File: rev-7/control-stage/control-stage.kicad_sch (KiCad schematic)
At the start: 65 parts, among them U1 REF4132A33, U2 ADP1706, U3 STM32G474RBTx, U4 LT3040, Y1 Crystal_GND24

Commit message: RC1 schematic + footprints
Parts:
- removed U1: REF4132A33, symbol rev-7-symbols:REF4132
- removed U4: LT3040, symbol rev-7-symbols:LT3040
- removed U?: (no value), symbol rev-7-symbols:ADP1706
- added C47, C48: DNP, Capacitor_SMD:C_0402_1005Metric, symbol Device:C_Small
- added C49: (no value), Capacitor_SMD:C_0402_1005Metric, symbol Device:C_Small
- added C50, C51, C52: (no value), symbol Device:C_Small
- added J5: (no value), symbol Connector_Generic:Conn_02x05_Counter_Clockwise
- added NT1: NetTie_2, symbol Device:NetTie_2
- added NT2: (no value), symbol Device:NetTie_2
- added R5, R8: (no value), symbol Device:R_Small_US
- added R6, R7, R9: 0, symbol Device:R_Small_US
- added U1: (no value), symbol rev-7-symbols:ADP7156ACPZ
- added U4: (no value), symbol Amplifier_Operational:TLV9004xRUCR
- C11, C9: value 20p -> (none); footprint Capacitor_SMD:C_0603_1608Metric -> (none)
- C22, C8: value 100n -> (none)
- C25: value 4.7u -> (none)
- C26: value 4.7u -> 1u
- C28: value 100n -> 1u
- C31: value 2.2u -> DNP; footprint (none) -> Capacitor_SMD:C_0402_1005Metric
- C5: value 4.7u -> (none); footprint (none) -> Capacitor_SMD:C_1210_3225Metric; P/N (none) -> GRM32EC81C476ME15L
- R2: value 200k -> (none)
- R3: value 5.1k -> (none)
- R4: value 499 -> (none)
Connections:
- net +3V3: now also J5.1 (Pin_1)
- net +3V3A: now also R4.2, C50.1, C51.1, C52.1, R5.1, U1.1 (VOUT), U1.2 (VOUT), U1.3 (VOUT_SENSE), U4.3 (V+)
- net +5V: now also J5.10 (Pin_10)
- net BOOT0: now also U3.61 (PB8), J5.8 (Pin_8)
- net CAN_RX: now also U3.58 (PB5); no longer U3.30 (PB10)
- net CAN_TX: now also U3.59 (PB6); no longer U3.62 (PB9)
- net DEBUG_RX: now also J5.7 (Pin_7)
- net DEBUG_SWCLK: now also J5.2 (Pin_2)
- net DEBUG_SWDIO: now also J5.9 (Pin_9)
- net DEBUG_TX: now also J5.4 (Pin_4)
- net EP: now also C31.2, R3.1, C47.2, C48.2, C49.2, C50.2, C51.2, C52.2, J5.5 (Pin_5), J5.6 (Pin_6), NT2.1, U1.11 (GND), U4.10 (V-); no longer C31.1, R4.1
- net NRST: now also J5.3 (Pin_3)
- net PGND: now also NT2.2
- net PHA_ISNS: now also U4.2 (+); no longer U3.12 (PA0)
- net PHB_ISNS: now also U4.4 (+); no longer U3.13 (PA1)
- net PHC_ISNS: now also U4.9 (+); no longer U3.25 (PB1)
- net THERM_A: now also R5.2
- net THERM_B: now also R4.1
- net VBUS: now also NT1.1
- net VBUS_VSNS: now also C5.1, R2.2, R3.2, U4.11 (+); no longer U3.36 (PB14)
- net V+: no longer names the net of C21.1, C7.1, C8.1, FB2.2
- net V+: now also C22.1, U1.10 (VIN), U1.5 (EN), U1.9 (VIN); no longer C25.1, C28.1, C5.1, R2.1
- new net: NT1.2, R2.1
- new net: R6.2, U4.1 (-), U4.14
- new net: R9.2, U4.5 (-), U4.6
- new net: R8.2, U4.12 (-), U4.13
- new net: C25.1, U1.4 (BYP)
- new net: C28.1, U1.6 (REF_SENSE), U1.7 (REF)
- new net: C26.1, U1.8 (VREG)
- new net: R7.2, U4.7, U4.8 (-)
- new net PHA_ISNS_BUF: C31.1, R6.1, U3.12 (PA0)
- new net PHB_ISNS_BUF: C47.1, R9.1, U3.13 (PA1)
- new net PHC_ISNS_BUF: C48.1, R7.1, U3.25 (PB1)
- new net VBUS_VSNS_BUF: C49.1, R8.1, U3.36 (PB14)
- no-connect marks 0 -> 22
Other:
- note added: "3V3 Analog LDO"
- note added: "3V3 Digital LDO"
- note added: "Analog"
- note added: "Analog Buffers"
- note added: "Debug"
- note added: "Inverter board +5V switch"
- note added: "Mezz plugs to inverter board"
- note added: "Op amp power"
- note added: "Phase/SPI"
- note added: "Power"
- note added: "STM32"
- note added: "Star at mezz"
- note added: "Up to 120mA draw - ~100-200mW TODO do we have the thermal conductivity for this not to be a problem? Should we use SMPS buck?"
- note removed: "3V3 +/- 2.5% 1A max"
- note removed: "hehe centipede"
- moved on the sheet: C1, C10, C11, C12, C13, C14, C15, C16, C17, C18, C19, C2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

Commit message: Design review changes
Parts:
- removed C10: 4.7u, symbol Device:C_Small
- removed C36: 22u, symbol Device:C_Small
- added C?: 4.7u, Capacitor_SMD:C_0603_1608Metric, symbol Device:C_Small
- added C?: 100n, Capacitor_SMD:C_0603_1608Metric, symbol Device:C_Small
- added R?: 120, Resistor_SMD:R_0603_1608Metric, symbol Device:R_Small_US
- added U?: TCAN330, project-footprints:SOT-23-8-Fixed, symbol Interface_CAN_LIN:TCAN330
- C11, C9: value (none) -> 18p; footprint (none) -> Capacitor_SMD:C_0402_1005Metric
- C12, C14, C52, C8: value (none) -> 4.7u; footprint (none) -> Capacitor_SMD:C_0603_1608Metric
- C13, C21, C3, C33, C34, C39, C4, C40, C41, C42: footprint (none) -> Capacitor_SMD:C_0603_1608Metric
- C15, C18, C26, C27, C28, C29, C30, C32, C38: footprint (none) -> Capacitor_SMD:C_0402_1005Metric
- C16: value (none) -> 10u; footprint (none) -> Capacitor_SMD:C_0603_1608Metric
- C17, C25, C37: value (none) -> 1u; footprint (none) -> Capacitor_SMD:C_0402_1005Metric
- C20: value (none) -> 1u; footprint (none) -> Capacitor_SMD:C_0603_1608Metric
- C22, C23, C24, C51: value (none) -> 100n; footprint (none) -> Capacitor_SMD:C_0402_1005Metric
- C35, C50: value (none) -> 10n; footprint (none) -> Capacitor_SMD:C_0402_1005Metric
- C43: footprint (none) -> Capacitor_SMD:C_0805_2012Metric
- C49: value (none) -> DNP
- C5: value (none) -> 10p
- FB1, FB2, FB4: footprint (none) -> Inductor_SMD:L_0603_1608Metric
- FB3: value (none) -> Z@1MHz=300ohm; footprint (none) -> Inductor_SMD:L_0603_1608Metric
- J1: value (none) -> MEZZ; footprint (none) -> rev-7-footprints:0555600307
- J2, J3, J4: value (none) -> 10132797-021100LF; footprint (none) -> rev-7-footprints:10132798-021100LF
- J5: value (none) -> PROG; footprint (none) -> Connector:Tag-Connect_TC2050-IDC-NL_2x05_P1.27mm_Vertical_with_bottom_clip
- NT1: footprint (none) -> NetTie:NetTie-2_SMD_Pad0.5mm
- NT2: value (none) -> NetTie_2; footprint (none) -> NetTie:NetTie-2_SMD_Pad0.5mm
- Q1: value (none) -> TPN4R712MD,L1Q; footprint (none) -> rev-7-footprints:TSON-Advance
- R1: value (none) -> 100k; footprint (none) -> Resistor_SMD:R_0402_1005Metric
- R2: value (none) -> 5.1k/0.1%; footprint (none) -> Resistor_SMD:R_0402_1005Metric
- R3: value (none) -> 3.3k/0.1%; footprint (none) -> Resistor_SMD:R_0402_1005Metric
- R4, R5: value (none) -> 100k/1%; footprint (none) -> Resistor_SMD:R_0402_1005Metric
- R6, R7, R9: footprint (none) -> Resistor_SMD:R_0402_1005Metric
- R8: value (none) -> 0; footprint (none) -> Resistor_SMD:R_0402_1005Metric
- U1: value (none) -> ADP7156ACPZ; footprint (none) -> Package_DFN_QFN:DFN-10-1EP_3x3mm_P0.5mm_EP1.55x2.48mm
- U4: value (none) -> TLV9154IRUCR; footprint (none) -> Package_DFN_QFN:Texas_S-PX2QFN-14
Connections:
- net IA_SNS is gone; now on net PHA_ISNS: J4.16 (Pin_16), J4.5 (Pin_5)
- net IB_SNS is gone; now on net PHB_ISNS: J4.14 (Pin_14), J4.7 (Pin_7)
- net IC_SNS is gone; now on net PHC_ISNS: J4.12 (Pin_12), J4.9 (Pin_9)
- net +3V3: now also C?.1, C?.1, U?.3 (VCC)
- net CAN_H: now also U?.7 (CANH)
- net CAN_L: now also U?.6 (CANL)
- net CAN_RX: now also U?.4 (RXD)
- net CAN_TX: now also U?.1 (TXD)
- net ENC_A: now also U3.8 (PC0)
- net ENC_B: now also U3.9 (PC1)
- net EP: now also C?.2, C?.2, U?.2 (GND), U?.8 (S)
- net SW_5V: now also U3.60 (PB7); no longer U3.34 (PB12)
- no-connect marks 22 -> 21
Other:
- note added: "5V tolerant"
- note added: "System Communications"
- moved on the sheet: C46, C5, R2, R3

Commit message: Pushing changes to rev7
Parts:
- removed C44, C45, C46: 47u, Capacitor_SMD:C_1210_3225Metric, symbol Device:C_Small
- removed C52: 4.7u, Capacitor_SMD:C_0603_1608Metric, symbol Device:C_Small
- removed J5: PROG, Connector:Tag-Connect_TC2050-IDC-NL_2x05_P1.27mm_Vertical_with_bottom_clip, symbol Connector_Generic:Conn_02x05_Counter_Clockwise
- removed R?: 120, Resistor_SMD:R_0603_1608Metric, symbol Device:R_Small_US
- added H1: Board_Def, rev-7-footprints:top-board-def, symbol Mechanical:MountingHole_Pad
- added J5: Hirose_FH12-10S-0.5SH, Connector_FFC-FPC:Hirose_FH12-10S-0.5SH_1x10-1MP_P0.50mm_Horizontal, symbol Connector_Generic_MountingPin:Conn_01x10_MountingPin
- U1: footprint Package_DFN_QFN:DFN-10-1EP_3x3mm_P0.5mm_EP1.55x2.48mm -> Package_DFN_QFN:DFN-10-1EP_3x3mm_P0.5mm_EP1.65x2.38mm
- U2: footprint (none) -> rev-7-footprints:DFN-8-1EP_3x3mm_P0.5mm_EP1.45x1.74mm
- U5: renamed from U?; footprint project-footprints:SOT-23-8-Fixed -> rev-7-footprints:SOT-23-8-Fixed
- gave numbers to parts that had none: 2
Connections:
- net +3V3: now also J5.1 (Pin_1)
- net +5V: now also J5.2 (Pin_2)
- net BOOT0: now also J5.7 (Pin_7)
- net DEBUG_RX: now also J5.9 (Pin_9)
- net DEBUG_SWCLK: now also J5.4 (Pin_4)
- net DEBUG_SWDIO: now also J5.5 (Pin_5)
- net DEBUG_TX: now also J5.8 (Pin_8)
- net NRST: now also J5.6 (Pin_6)
- net BYP: now reaches C25.1, U1.4 (BYP)
- net REF: now reaches C28.1, U1.6 (REF_SENSE), U1.7 (REF)
- net VREG: now reaches C26.1, U1.8 (VREG)
- net EP renamed GND
- net GND: now also J5.10 (Pin_10), J5.3 (Pin_3), J5.MP (MountPin)
- new net CHASSIS: H1.1
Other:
- note removed: "System Communications"

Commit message: Updating
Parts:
- removed C31, C47, C48, C49: DNP, Capacitor_SMD:C_0402_1005Metric, symbol Device:C_Small
- removed C50: 10n, Capacitor_SMD:C_0402_1005Metric, symbol Device:C_Small
- removed C51: 100n, Capacitor_SMD:C_0402_1005Metric, symbol Device:C_Small
- removed R6, R7, R8, R9: 0, Resistor_SMD:R_0402_1005Metric, symbol Device:R_Small_US
- removed U4: TLV9154IRUCR, Package_DFN_QFN:Texas_S-PX2QFN-14, symbol Amplifier_Operational:TLV9004xRUCR
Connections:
- net PHA_ISNS_BUF is gone; now on net PHA_ISNS: U3.12 (PA0)
- net PHB_ISNS_BUF is gone; now on net PHB_ISNS: U3.13 (PA1)
- net PHC_ISNS_BUF is gone; now on net PHC_ISNS: U3.25 (PB1)
- net VBUS_VSNS_BUF is gone; now on net VBUS_VSNS: U3.36 (PB14)
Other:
- note added: "Swap with MEMS?"
- note removed: "Analog Buffers"
- note removed: "Op amp power"

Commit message: Rev 7 RC1 - Push before design review
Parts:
- removed C21, C33, C34, C40, C41, C42: 4.7u, Capacitor_SMD:C_0603_1608Metric, symbol Device:C_Small
- removed C30: 100n, Capacitor_SMD:C_0402_1005Metric, symbol Device:C_Small
- removed C39: 10u, Capacitor_SMD:C_0603_1608Metric, symbol Device:C_Small
- removed C43: 22u, Capacitor_SMD:C_0805_2012Metric, symbol Device:C_Small
- removed FB2: Z@1MHz=100ohm, Inductor_SMD:L_0603_1608Metric, symbol Device:FerriteBead_Small
- removed FB3, FB4: Z@1MHz=300ohm, Inductor_SMD:L_0603_1608Metric, symbol Device:FerriteBead_Small
- removed NT1: NetTie_2, NetTie:NetTie-2_SMD_Pad0.5mm, symbol Device:NetTie_2
- removed U2: ADP1706, rev-7-footprints:DFN-8-1EP_3x3mm_P0.5mm_EP1.45x1.74mm, symbol rev-7-symbols:ADP1706
- added L1: 2.2u, Inductor_SMD:L_1008_2520Metric, symbol Device:L
- added NT3: NetTie_2, NetTie:NetTie-2_SMD_Pad0.5mm, symbol Device:NetTie_2
- added R10: 100k/1%, Resistor_SMD:R_0402_1005Metric, symbol Device:R_Small_US
- added R11, R12, R13, R14, R15, R16, R17, R18, R19: THJP0603ABT1, Resistor_SMD:R_0603_1608Metric, symbol Device:R_Small_US
- added R6, R7: 10k, Resistor_SMD:R_0402_1005Metric, symbol Device:R_Small_US
- added R8: 2.2, Resistor_SMD:R_0603_1608Metric, symbol Device:R_Small_US
- added R9: 442k/1%, Resistor_SMD:R_0402_1005Metric, symbol Device:R_Small_US
- added U2: TLV62569DRL, Package_TO_SOT_SMD:SOT-563, symbol Regulator_Switching:TLV62569DRL
- C10, C4, C8: value 4.7u -> 10u; P/N (none) -> GRT188R61C106KE13
- C11, C9: value 18p -> 20p
- C12, C13: value 4.7u -> 22u; P/N (none) -> GRT188C80J226ME13D
- C15: value 100n -> 22u; footprint Capacitor_SMD:C_0402_1005Metric -> Capacitor_SMD:C_0603_1608Metric; P/N (none) -> GRT188C80J226ME13D
- C16: value 10u -> 22u; P/N (none) -> GRT188C80J226ME13D
- C17: value 1u -> 22u; footprint Capacitor_SMD:C_0402_1005Metric -> Capacitor_SMD:C_0603_1608Metric; P/N (none) -> GRT188C80J226ME13D
- C18: value 10n -> DNP
- C20, C36: footprint Capacitor_SMD:C_0603_1608Metric -> Capacitor_SMD:C_0402_1005Metric
- C24: value 100n -> 10n
- C3: value 4.7u -> 100n; footprint Capacitor_SMD:C_0603_1608Metric -> Capacitor_SMD:C_0402_1005Metric
- C5: footprint Capacitor_SMD:C_1210_3225Metric -> Capacitor_SMD:C_0402_1005Metric
- C6, C7: value 47u -> 10u; footprint Capacitor_SMD:C_1210_3225Metric -> Capacitor_SMD:C_0603_1608Metric; P/N GRM32EC81C476ME15L -> GRT188R61C106KE13
- FB1: value Z@1MHz=100ohm -> MPZ1608B471ATA00
- Y1: footprint Crystal:Crystal_SMD_3225-4Pin_3.2x2.5mm -> Crystal:Crystal_SMD_2016-4Pin_2.0x1.6mm; P/N ABM8-16.000MHZ-10-1-U-T -> ECS-160-12-37BQ-CTN-TR
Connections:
- net SPI_NSS is gone; now on net SPI_nCS: U3.18 (PA4)
- net +3V3: now also C12.2, C13.2, C18.1, C3.2, L1.2, R6.1, R9.2; no longer C10.1, C17.2
- net +3V3A: now also C15.2, C16.2, C17.2, C20.1, C24.1, C35.2, C37.2, U3.28 (VREF+), U3.29 (VDDA); no longer C12.1
- net +5V: now also C6.1, R8.1, U2.3 (VIN), U2.5 (EN); no longer C3.1, FB1.1
- net +5V_SW: now also R19.1
- net BOOT0: now also R7.1
- net CHASSIS: now also R11.1, R12.1, R13.1, R14.1, R15.1, R16.1, R17.1, R18.1
- net GND: now also C12.1, C13.1, C15.1, C16.1, C3.1, NT2.2, NT3.1, R11.2, R12.2, R13.2, R14.2, R15.2, R16.2, R17.2, R18.2, R19.2, R7.2, U2.2 (GND); no longer C1.2, C12.2, C13.2, C15.2, C16.2, C18.2, C3.2, J1.10 (Pin_10), J1.11 (Pin_11), J1.12 (Pin_12), J1.13 (Pin_13), J1.14 (Pin_14), J1.15 (Pin_15), J1.16 (Pin_16), J1.9 (Pin_9), J5.3 (Pin_3), NT2.1
- net NRST: now also R6.2
- net PGND: now also C1.2, J1.10 (Pin_10), J1.11 (Pin_11), J1.12 (Pin_12), J1.13 (Pin_13), J1.14 (Pin_14), J1.15 (Pin_15), J1.16 (Pin_16), J1.9 (Pin_9), NT2.1; no longer NT2.2
- net VBUS: now also R2.1
- net at C22.1, C7.1, C8.1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: now also C10.1, FB1.2
- net DEBUG_SWO: now reaches U3.56 (PB3)
- net DEBUG_SWO: now also J5.3 (Pin_3)
- net CAN_H renamed CAN_P
- net CAN_L renamed CAN_N
- removed net IN: C13.1, C15.1, C6.1, FB1.2
- new net: L1.1, U2.4 (SW)
- new net: FB1.1, R8.2
- new net FB: C18.2, R10.2, R9.1, U2.1 (FB)
- new net GNDS: NT3.2, R10.1
- no-connect marks 21 -> 20
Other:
- note added: "3V3 Digital SMPS"
- note added: "8u/ea derated"
- note added: "BOM"
- note added: "Thermal Jumpers"
- note added: "Thermal jumper"
- note added: "Use TLV62569A if possible - CCM for lower ripple"
- note added: "check if 5V tolerant"
- note removed: "3V3 Digital LDO"
- note removed: "Up to 120mA draw - ~100-200mW TODO do we have the thermal conductivity for this not to be a problem? Should we use SMPS buck?"
- moved on the sheet: C11, C14, C2, C20, C22, C25, C26, C28, C36, C38, C4, C9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

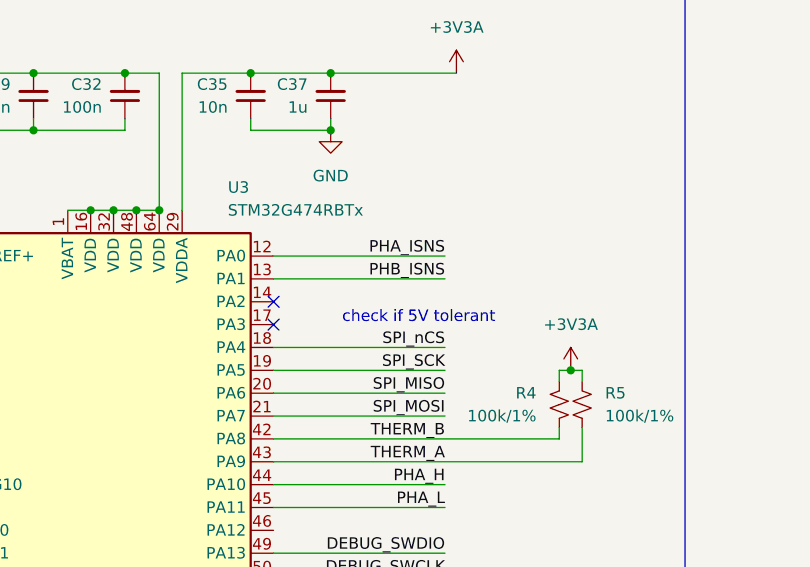
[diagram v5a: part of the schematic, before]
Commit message: unfucked via, added text note
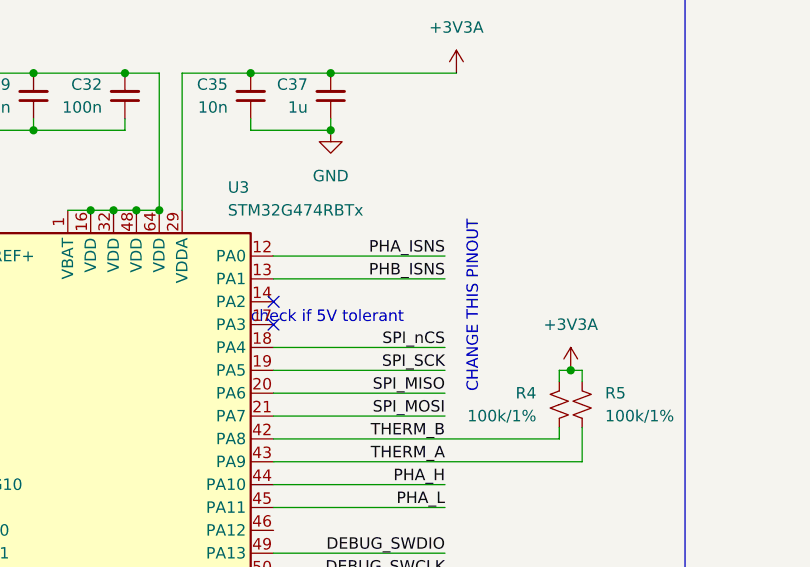
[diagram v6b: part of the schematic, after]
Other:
- note added: "CHANGE THIS PINOUT"
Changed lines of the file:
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@@
     (effects (font (size 2 2)) (justify left bottom))
   )
-  (text "check if 5V tolerant" (at 189.23 160.02 0)
+  (text "CHANGE THIS PINOUT " (at 204.47 167.64 90)
     (effects (font (size 1.27 1.27)) (justify left bottom))
   )
+  (text "check if 5V tolerant" (at 179.07 160.02 0)
+    (effects (font (size 1.27 1.27)) (justify left bottom))
+  )

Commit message: Switch to running mag encoder on 3v3, move to OResat standard debug connector
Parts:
- removed J5: Hirose_FH12-10S-0.5SH, Connector_FFC-FPC:Hirose_FH12-10S-0.5SH_1x10-1MP_P0.50mm_Horizontal, symbol Connector_Generic_MountingPin:Conn_01x10_MountingPin
- added J6: J-TE-Debug-2-1734592-0, rev-7-footprints:J-TE_2-1734592-0, symbol rev-7-symbols:J-TE-Debug-2-1734592-0
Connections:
- net +3V3: now also J3.10 (Pin_10), J3.11 (Pin_11), J6.11 (VTARGET)
- net +5V: now also J6.1 (VBUSP), J6.2 (VBUSP)
- net BOOT0: now also J6.19 (DEBUG-2)
- net DEBUG_RX: now also J6.18 (DEBUG-1)
- net DEBUG_SWCLK: now also J6.15 (SWCLK)
- net DEBUG_SWDIO: now also J6.14 (SWDIO)
- net DEBUG_SWO: now also J6.16 (SWO)
- net DEBUG_TX: now also J6.17 (DEBUG-0)
- net GND: now also J6.3 (GND), J6.6 (GND), J6.9 (GND), J6.PAD1 (PAD), J6.PAD2 (PAD); no longer J3.10 (Pin_10), J3.11 (Pin_11)
- net NRST: now also J6.10 (NRST)
- no-connect marks 20 -> 26
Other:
- moved on the sheet: H1, R11, R12, R13, R14, R15, R16, R17, R18, R6

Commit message: Rev 7 Release
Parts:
- removed R19: THJP0603ABT1, Resistor_SMD:R_0603_1608Metric, symbol Device:R_Small_US
- added C21: 22u, Capacitor_SMD:C_0603_1608Metric, symbol Device:C_Small
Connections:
- net +3V3: now also Q1.1 (S), R1.1; no longer J3.10 (Pin_10), J3.11 (Pin_11)
- net +5V: now also J2.10 (Pin_10), J2.11 (Pin_11), J2.12 (Pin_12), J2.9 (Pin_9); no longer Q1.1 (S), R1.1
- net DEBUG_RX: now also J6.12 (CARD-RX)
- net DEBUG_TX: now also J6.13 (CARD-TX)
- net GND: now also C21.1
- net SW_3V3: now reaches U3.17 (PA3)
- net SW_3V3: now also Q1.2 (G), R1.2
- removed net +5V_SW: J2.10 (Pin_10), J2.11 (Pin_11), J2.12 (Pin_12), J2.9 (Pin_9), Q1.3 (D)
- removed net SW_5V: Q1.2 (G), R1.2, U3.60 (PB7)
- new net +3V3_SW: C21.2, J3.10 (Pin_10), J3.11 (Pin_11), Q1.3 (D)
- no-connect marks 26 -> 23
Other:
- note added: "Encoder power switch"
- note added: "wheeeeeee"
- note removed: "CHANGE THIS PINOUT"
- note removed: "Thermal jumper"
- note removed: "check if 5V tolerant"
